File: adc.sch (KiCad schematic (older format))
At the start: 18 parts, among them U28 AD7961BCPZ-RL7, U29 OPA325

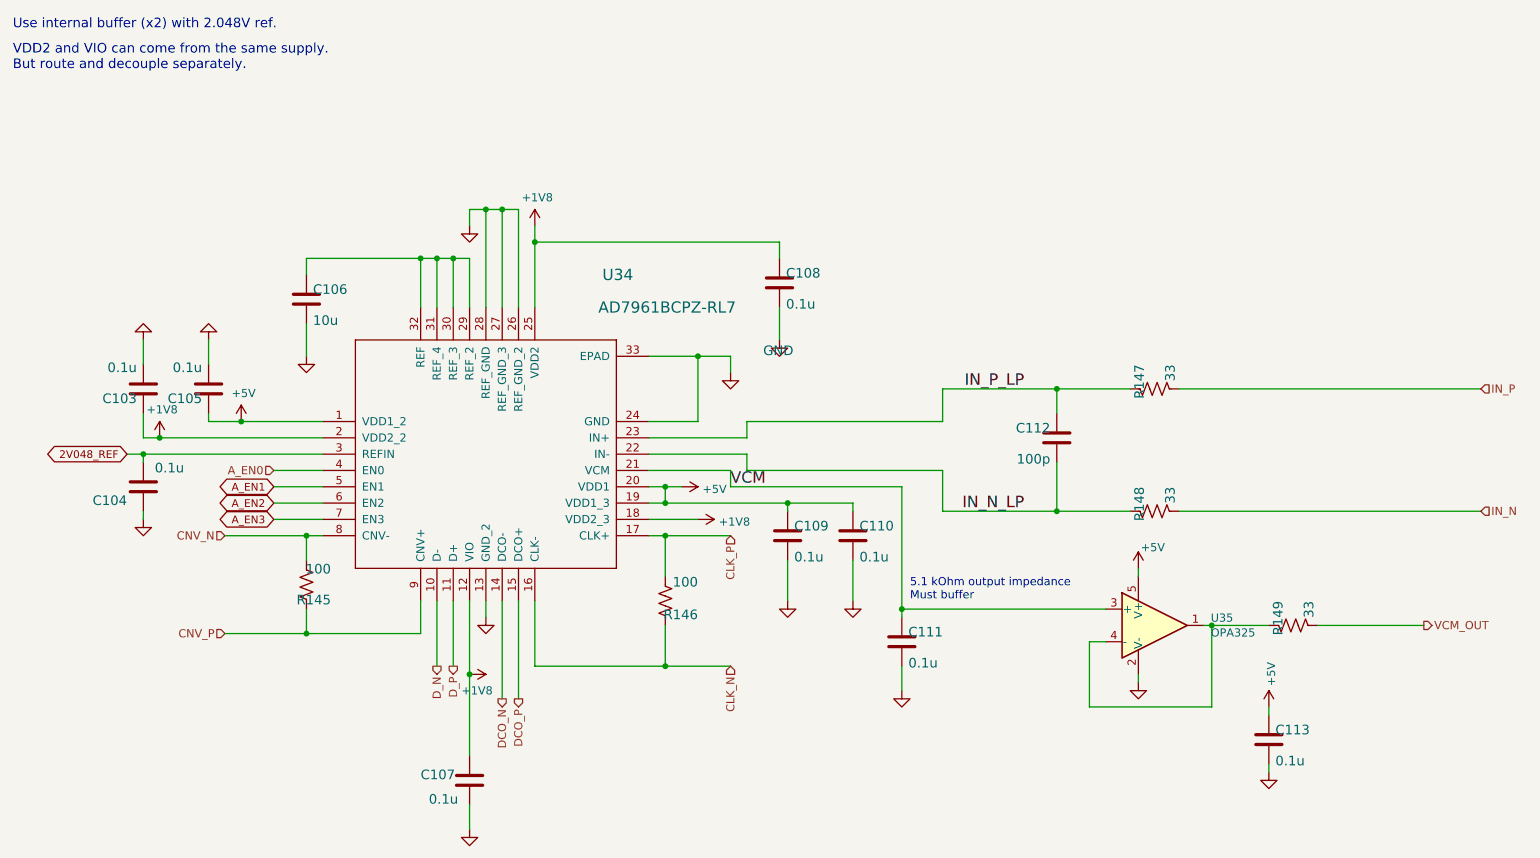
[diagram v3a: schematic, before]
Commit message: move around signals for easier routing
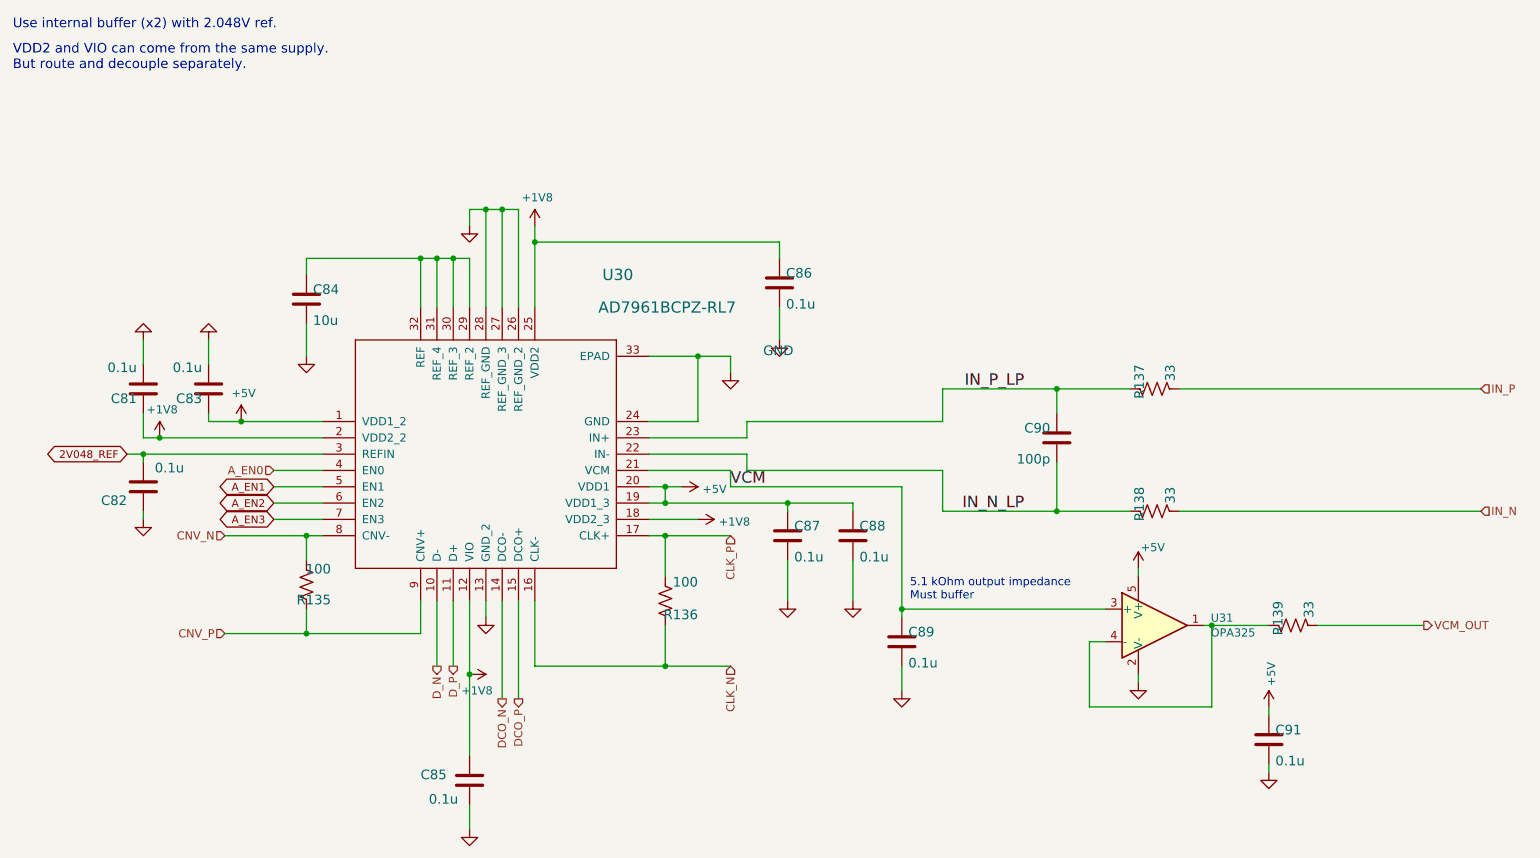
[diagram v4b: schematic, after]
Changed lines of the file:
@@
 AR Path="/60BF7757/B0DC2316" Ref="C101"  Part="1"
 AR Path="/60C1F416/B0DC2316" Ref="C112"  Part="1"
-F 0 "C112" H 7090 3725 59  0000 L BNN
+F 0 "C90" H 7090 3725 59  0000 L BNN
 F 1 "100p" H 7090 3535 59  0000 L BNN
 F 2 "Capacitor_SMD:C_0603_1608Metric" H 7050 3700 50  0001 C CNN
@@
 AR Path="/60BF7757/B996151F" Ref="R140"  Part="1"
 AR Path="/60C1F416/B996151F" Ref="R145"  Part="1"
-F 0 "R145" H 2300 4659 59  0000 L BNN
+F 0 "R135" H 2300 4659 59  0000 L BNN
 F 1 "100" H 2300 4470 59  0000 L BNN
 F 2 "Resistor_SMD:R_0603_1608Metric" H 2450 4600 50  0001 C CNN
@@
 AR Path="/60BF7757/56DFCCD0" Ref="C97"  Part="1"
 AR Path="/60C1F416/56DFCCD0" Ref="C108"  Part="1"
-F 0 "C108" H 5390 2775 59  0000 L BNN
+F 0 "C86" H 5390 2775 59  0000 L BNN
 F 1 "0.1u" H 5390 2585 59  0000 L BNN
 F 2 "Capacitor_SMD:C_0603_1608Metric" H 5350 2750 50  0001 C CNN
@@
 AR Path="/60BF7757/BF33D434" Ref="R141"  Part="1"
 AR Path="/60C1F416/BF33D434" Ref="R146"  Part="1"
-F 0 "R146" H 4450 4750 59  0000 L BNN
+F 0 "R136" H 4450 4750 59  0000 L BNN
 F 1 "100" H 4450 4550 59  0000 L BNN
 F 2 "Resistor_SMD:R_0603_1608Metric" H 4650 4700 50  0001 C CNN
@@
 AR Path="/60BF7757/C9238E33" Ref="C98"  Part="1"
 AR Path="/60C1F416/C9238E33" Ref="C109"  Part="1"
-F 0 "C109" H 5440 4325 59  0000 L BNN
+F 0 "C87" H 5440 4325 59  0000 L BNN
 F 1 "0.1u" H 5440 4135 59  0000 L BNN
 F 2 "Capacitor_SMD:C_0603_1608Metric" H 5400 4300 50  0001 C CNN
@@
 AR Path="/60BF7757/E612D2BB" Ref="C99"  Part="1"
 AR Path="/60C1F416/E612D2BB" Ref="C110"  Part="1"
-F 0 "C110" H 5840 4325 59  0000 L BNN
+F 0 "C88" H 5840 4325 59  0000 L BNN
 F 1 "0.1u" H 5840 4135 59  0000 L BNN
 F 2 "Capacitor_SMD:C_0603_1608Metric" H 5800 4300 50  0001 C CNN
@@
 AR Path="/60BF7757/1FADEAAB" Ref="C92"  Part="1"
 AR Path="/60C1F416/1FADEAAB" Ref="C103"  Part="1"
-F 0 "C103" H 1490 3425 59  0000 L BNN
+F 0 "C81" H 1490 3425 59  0000 L BNN
 F 1 "0.1u" H 1490 3235 59  0000 L BNN
 F 2 "Capacitor_SMD:C_0603_1608Metric" H 1450 3400 50  0001 C CNN
@@
 AR Path="/60BF7757/9D5B9004" Ref="C94"  Part="1"
 AR Path="/60C1F416/9D5B9004" Ref="C105"  Part="1"
-F 0 "C105" H 1890 3425 59  0000 L BNN
+F 0 "C83" H 1890 3425 59  0000 L BNN
 F 1 "0.1u" H 1890 3235 59  0000 L BNN
 F 2 "Capacitor_SMD:C_0603_1608Metric" H 1850 3400 50  0001 C CNN
@@
 AR Path="/60BF7757/87DF8B8E" Ref="R142"  Part="1"
 AR Path="/60C1F416/87DF8B8E" Ref="R147"  Part="1"
-F 0 "R147" H 7500 3459 59  0000 L BNN
+F 0 "R137" H 7500 3459 59  0000 L BNN
 F 1 "33" H 7500 3270 59  0000 L BNN
 F 2 "Resistor_SMD:R_0603_1608Metric" H 7650 3400 50  0001 C CNN
@@
 AR Path="/60BF7757/BFC3FA38" Ref="R143"  Part="1"
 AR Path="/60C1F416/BFC3FA38" Ref="R148"  Part="1"
-F 0 "R148" H 7500 4209 59  0000 L BNN
+F 0 "R138" H 7500 4209 59  0000 L BNN
 F 1 "33" H 7500 4020 59  0000 L BNN
 F 2 "Resistor_SMD:R_0603_1608Metric" H 7650 4150 50  0001 C CNN
@@
 AR Path="/60BF7757/E8572435" Ref="C96"  Part="1"
 AR Path="/60C1F416/E8572435" Ref="C107"  Part="1"
-F 0 "C107" H 3150 5800 59  0000 L BNN
+F 0 "C85" H 3150 5800 59  0000 L BNN
 F 1 "0.1u" H 3200 5650 59  0000 L BNN
 F 2 "Capacitor_SMD:C_0603_1608Metric" H 3450 5800 50  0001 C CNN
@@
 AR Path="/60BF7757/70C280EF" Ref="U32"  Part="1"
 AR Path="/60C1F416/70C280EF" Ref="U34"  Part="1"
-F 0 "U34" H 4264 4859 69  0000 L BNN
+F 0 "U30" H 4264 4859 69  0000 L BNN
 F 1 "AD7961BCPZ-RL7" H 4239 4659 69  0000 L BNN
 F 2 "Package_DFN_QFN:QFN-32-1EP_5x5mm_P0.5mm_EP3.1x3.1mm" H 3550 3800 50  0001 C CNN
@@
 AR Path="/60BF7757/32508C8E" Ref="C95"  Part="1"
 AR Path="/60C1F416/32508C8E" Ref="C106"  Part="1"
-F 0 "C106" H 2490 2875 59  0000 L BNN
+F 0 "C84" H 2490 2875 59  0000 L BNN
 F 1 "10u" H 2490 2685 59  0000 L BNN
 F 2 "Capacitor_SMD:C_0603_1608Metric" H 2450 2850 50  0001 C CNN
@@
 AR Path="/60BF7757/60CEDBBA" Ref="U33"  Part="1"
 AR Path="/60C1F416/60CEDBBA" Ref="U35"  Part="1"
-F 0 "U35" H 7994 4896 50  0000 L CNN
+F 0 "U31" H 7994 4896 50  0000 L CNN
 F 1 "OPA325" H 7994 4805 50  0000 L CNN
 F 2 "Package_TO_SOT_SMD:SOT-23-5" H 7550 4650 50  0001 L CNN
@@
 AR Path="/60BF7757/60D076A5" Ref="R144"  Part="1"
 AR Path="/60C1F416/60D076A5" Ref="R149"  Part="1"
-F 0 "R149" H 8350 4909 59  0000 L BNN
+F 0 "R139" H 8350 4909 59  0000 L BNN
 F 1 "33" H 8350 4720 59  0000 L BNN
 F 2 "Resistor_SMD:R_0603_1608Metric" H 8500 4850 50  0001 C CNN
@@
 AR Path="/60BF7757/60D0F62A" Ref="C102"  Part="1"
 AR Path="/60C1F416/60D0F62A" Ref="C113"  Part="1"
-F 0 "C113" H 8390 5575 59  0000 L BNN
+F 0 "C91" H 8390 5575 59  0000 L BNN
 F 1 "0.1u" H 8390 5385 59  0000 L BNN
 F 2 "Capacitor_SMD:C_0603_1608Metric" H 8350 5550 50  0001 C CNN
@@
 AR Path="/60BF7757/60D49EBB" Ref="C93"  Part="1"
 AR Path="/60C1F416/60D49EBB" Ref="C104"  Part="1"
-F 0 "C104" H 1550 4050 59  0000 L BNN
+F 0 "C82" H 1550 4050 59  0000 L BNN
 F 1 "0.1u" H 1200 3850 59  0000 L BNN
 F 2 "Capacitor_SMD:C_0603_1608Metric" H 1450 4000 50  0001 C CNN
@@
 AR Path="/60BF7757/60D51F18" Ref="C100"  Part="1"
 AR Path="/60C1F416/60D51F18" Ref="C111"  Part="1"
-F 0 "C111" H 6140 4975 59  0000 L BNN
+F 0 "C89" H 6140 4975 59  0000 L BNN
 F 1 "0.1u" H 6140 4785 59  0000 L BNN
 F 2 "Capacitor_SMD:C_0603_1608Metric" H 6100 4950 50  0001 C CNN

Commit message: before importing autoroute
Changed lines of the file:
@@
 $Descr A 11000 8500
 encoding utf-8
-Sheet 12 26
+Sheet 10 26
 Title ""
 Date ""
@@
 AR Path="/60BF7757/B0DC2316" Ref="C101"  Part="1"
 AR Path="/60C1F416/B0DC2316" Ref="C112"  Part="1"
-F 0 "C90" H 7090 3725 59  0000 L BNN
+F 0 "C47" H 7090 3725 59  0000 L BNN
 F 1 "100p" H 7090 3535 59  0000 L BNN
 F 2 "Capacitor_SMD:C_0603_1608Metric" H 7050 3700 50  0001 C CNN
@@
 AR Path="/60BF7757/B996151F" Ref="R140"  Part="1"
 AR Path="/60C1F416/B996151F" Ref="R145"  Part="1"
-F 0 "R135" H 2300 4659 59  0000 L BNN
+F 0 "R79" H 2300 4659 59  0000 L BNN
 F 1 "100" H 2300 4470 59  0000 L BNN
 F 2 "Resistor_SMD:R_0603_1608Metric" H 2450 4600 50  0001 C CNN
@@
 AR Path="/60BF7757/56DFCCD0" Ref="C97"  Part="1"
 AR Path="/60C1F416/56DFCCD0" Ref="C108"  Part="1"
-F 0 "C86" H 5390 2775 59  0000 L BNN
+F 0 "C43" H 5390 2775 59  0000 L BNN
 F 1 "0.1u" H 5390 2585 59  0000 L BNN
 F 2 "Capacitor_SMD:C_0603_1608Metric" H 5350 2750 50  0001 C CNN
@@
 AR Path="/60BF7757/BF33D434" Ref="R141"  Part="1"
 AR Path="/60C1F416/BF33D434" Ref="R146"  Part="1"
-F 0 "R136" H 4450 4750 59  0000 L BNN
+F 0 "R80" H 4450 4750 59  0000 L BNN
 F 1 "100" H 4450 4550 59  0000 L BNN
 F 2 "Resistor_SMD:R_0603_1608Metric" H 4650 4700 50  0001 C CNN
@@
 AR Path="/60BF7757/C9238E33" Ref="C98"  Part="1"
 AR Path="/60C1F416/C9238E33" Ref="C109"  Part="1"
-F 0 "C87" H 5440 4325 59  0000 L BNN
+F 0 "C44" H 5440 4325 59  0000 L BNN
 F 1 "0.1u" H 5440 4135 59  0000 L BNN
 F 2 "Capacitor_SMD:C_0603_1608Metric" H 5400 4300 50  0001 C CNN
@@
 AR Path="/60BF7757/E612D2BB" Ref="C99"  Part="1"
 AR Path="/60C1F416/E612D2BB" Ref="C110"  Part="1"
-F 0 "C88" H 5840 4325 59  0000 L BNN
+F 0 "C45" H 5840 4325 59  0000 L BNN
 F 1 "0.1u" H 5840 4135 59  0000 L BNN
 F 2 "Capacitor_SMD:C_0603_1608Metric" H 5800 4300 50  0001 C CNN
@@
 AR Path="/60BF7757/1FADEAAB" Ref="C92"  Part="1"
 AR Path="/60C1F416/1FADEAAB" Ref="C103"  Part="1"
-F 0 "C81" H 1490 3425 59  0000 L BNN
+F 0 "C38" H 1490 3425 59  0000 L BNN
 F 1 "0.1u" H 1490 3235 59  0000 L BNN
 F 2 "Capacitor_SMD:C_0603_1608Metric" H 1450 3400 50  0001 C CNN
@@
 AR Path="/60BF7757/9D5B9004" Ref="C94"  Part="1"
 AR Path="/60C1F416/9D5B9004" Ref="C105"  Part="1"
-F 0 "C83" H 1890 3425 59  0000 L BNN
+F 0 "C40" H 1890 3425 59  0000 L BNN
 F 1 "0.1u" H 1890 3235 59  0000 L BNN
 F 2 "Capacitor_SMD:C_0603_1608Metric" H 1850 3400 50  0001 C CNN
@@
 AR Path="/60BF7757/87DF8B8E" Ref="R142"  Part="1"
 AR Path="/60C1F416/87DF8B8E" Ref="R147"  Part="1"
-F 0 "R137" H 7500 3459 59  0000 L BNN
+F 0 "R81" H 7500 3459 59  0000 L BNN
 F 1 "33" H 7500 3270 59  0000 L BNN
 F 2 "Resistor_SMD:R_0603_1608Metric" H 7650 3400 50  0001 C CNN
@@
 AR Path="/60BF7757/BFC3FA38" Ref="R143"  Part="1"
 AR Path="/60C1F416/BFC3FA38" Ref="R148"  Part="1"
-F 0 "R138" H 7500 4209 59  0000 L BNN
+F 0 "R82" H 7500 4209 59  0000 L BNN
 F 1 "33" H 7500 4020 59  0000 L BNN
 F 2 "Resistor_SMD:R_0603_1608Metric" H 7650 4150 50  0001 C CNN
@@
 AR Path="/60BF7757/E8572435" Ref="C96"  Part="1"
 AR Path="/60C1F416/E8572435" Ref="C107"  Part="1"
-F 0 "C85" H 3150 5800 59  0000 L BNN
+F 0 "C42" H 3150 5800 59  0000 L BNN
 F 1 "0.1u" H 3200 5650 59  0000 L BNN
 F 2 "Capacitor_SMD:C_0603_1608Metric" H 3450 5800 50  0001 C CNN
@@
 AR Path="/60BF7757/70C280EF" Ref="U32"  Part="1"
 AR Path="/60C1F416/70C280EF" Ref="U34"  Part="1"
-F 0 "U30" H 4264 4859 69  0000 L BNN
+F 0 "U28" H 4264 4859 69  0000 L BNN
 F 1 "AD7961BCPZ-RL7" H 4239 4659 69  0000 L BNN
 F 2 "Package_DFN_QFN:QFN-32-1EP_5x5mm_P0.5mm_EP3.1x3.1mm" H 3550 3800 50  0001 C CNN
@@
 AR Path="/60BF7757/32508C8E" Ref="C95"  Part="1"
 AR Path="/60C1F416/32508C8E" Ref="C106"  Part="1"
-F 0 "C84" H 2490 2875 59  0000 L BNN
+F 0 "C41" H 2490 2875 59  0000 L BNN
 F 1 "10u" H 2490 2685 59  0000 L BNN
 F 2 "Capacitor_SMD:C_0603_1608Metric" H 2450 2850 50  0001 C CNN
@@
 AR Path="/60BF7757/60CEDBBA" Ref="U33"  Part="1"
 AR Path="/60C1F416/60CEDBBA" Ref="U35"  Part="1"
-F 0 "U31" H 7994 4896 50  0000 L CNN
+F 0 "U29" H 7994 4896 50  0000 L CNN
 F 1 "OPA325" H 7994 4805 50  0000 L CNN
 F 2 "Package_TO_SOT_SMD:SOT-23-5" H 7550 4650 50  0001 L CNN
@@
 AR Path="/60BF7757/60D076A5" Ref="R144"  Part="1"
 AR Path="/60C1F416/60D076A5" Ref="R149"  Part="1"
-F 0 "R139" H 8350 4909 59  0000 L BNN
+F 0 "R83" H 8350 4909 59  0000 L BNN
 F 1 "33" H 8350 4720 59  0000 L BNN
 F 2 "Resistor_SMD:R_0603_1608Metric" H 8500 4850 50  0001 C CNN
@@
 AR Path="/60BF7757/60D0F62A" Ref="C102"  Part="1"
 AR Path="/60C1F416/60D0F62A" Ref="C113"  Part="1"
-F 0 "C91" H 8390 5575 59  0000 L BNN
+F 0 "C48" H 8390 5575 59  0000 L BNN
 F 1 "0.1u" H 8390 5385 59  0000 L BNN
 F 2 "Capacitor_SMD:C_0603_1608Metric" H 8350 5550 50  0001 C CNN
@@
 AR Path="/60BF7757/60D49EBB" Ref="C93"  Part="1"
 AR Path="/60C1F416/60D49EBB" Ref="C104"  Part="1"
-F 0 "C82" H 1550 4050 59  0000 L BNN
+F 0 "C39" H 1550 4050 59  0000 L BNN
 F 1 "0.1u" H 1200 3850 59  0000 L BNN
 F 2 "Capacitor_SMD:C_0603_1608Metric" H 1450 4000 50  0001 C CNN
@@
 AR Path="/60BF7757/60D51F18" Ref="C100"  Part="1"
 AR Path="/60C1F416/60D51F18" Ref="C111"  Part="1"
-F 0 "C89" H 6140 4975 59  0000 L BNN
+F 0 "C46" H 6140 4975 59  0000 L BNN
 F 1 "0.1u" H 6140 4785 59  0000 L BNN
 F 2 "Capacitor_SMD:C_0603_1608Metric" H 6100 4950 50  0001 C CNN

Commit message: move bom files to bom folder
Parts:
- C42, C45: Tolerance (none) -> 10%; Voltage (none) -> 25
- C44: Voltage (none) -> 25; voltage 25 -> (none)
- U28: symbol covg-kicad:AD7960BCPZ-RL7 -> covg-kicad:AD7961BCPZ-RL7
